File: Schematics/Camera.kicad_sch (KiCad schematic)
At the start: 7 parts, among them U2 TPS22917DBVR

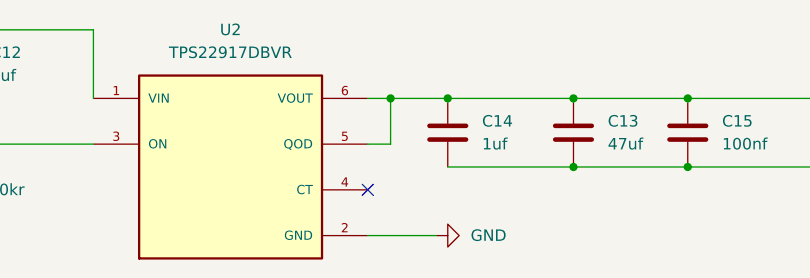
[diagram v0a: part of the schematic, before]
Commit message: Ran ERC added Pwr Flags
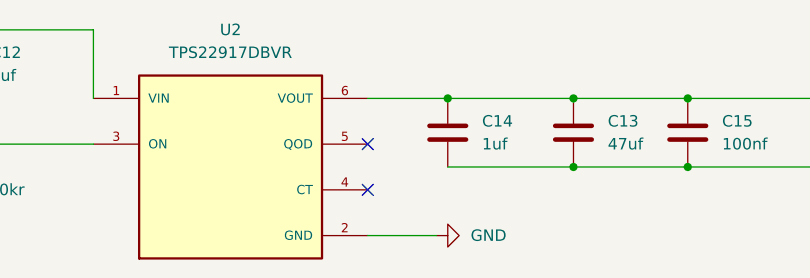
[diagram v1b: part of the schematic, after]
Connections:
- net at C13.1, C14.1, C15.1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: no longer U2.5 (QOD)
- no-connect marks 1 -> 2
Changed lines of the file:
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@@
-		(color 0 0 0 0)
-	)
-	(junction
-		(at 106.68 90.17)
-		(diameter 0)
 		(color 0 0 0 0)
 	)
 	(no_connect
+		(at 104.14 95.25)
+	)
+	(no_connect
 		(at 104.14 100.33)
-	)
-	(wire
-		(pts
-			(xy 104.14 95.25) (xy 106.68 95.25)
-		)
-		(stroke
-			(width 0)
-			(type default)
-		)
 	)
 	(wire
@@
 	(wire
 		(pts
-			(xy 106.68 95.25) (xy 106.68 90.17)
-		)
-		(stroke
-			(width 0)
-			(type default)
-		)
-	)
-	(wire
-		(pts
 			(xy 173.99 96.52) (xy 214.63 96.52)
 		)
@@
 	(wire
 		(pts
-			(xy 106.68 90.17) (xy 113.03 90.17)
+			(xy 104.14 90.17) (xy 113.03 90.17)
 		)
 		(stroke
@@
 		)
 		(stroke
-			(width 0)
-			(type default)
-		)
-	)
-	(wire
-		(pts
-			(xy 104.14 90.17) (xy 106.68 90.17)
-		)
-		(stroke

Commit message: final design pcb
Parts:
- renumbered C12 to C18, C14 to C19, C13 to C20, C15 to C21, R2 to R5, U2 to U3
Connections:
- net +5V renamed Cam5v
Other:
- moved on the sheet: C19, C20, C21
